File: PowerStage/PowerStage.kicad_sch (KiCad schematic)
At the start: 90 parts, among them J1 AH, J10 AH, J11 AH, J12 AH, J13 AH, J14 AH, J19 PhaseA, J2 AH, J20 PhaseB, J21 PhaseB, J22 AH, J23 AH, J24 AH, J25 AH, J3 BH, J4 BH, J5 BH, J6 CH, J7 CH, J8 CH, J9 AH, Q20 HY5110W, Q21 HY5110W, Q22 HY5110W, Q23 HY5110W, Q24 HY5110W, Q25 HY5110W, Q26 HY5110W, Q27 HY5110W, Q28 HY5110W, Q29 HY5110W, Q30 HY5110W, Q31 HY5110W, Q38 HY5110W, Q39 HY5110W, Q40 HY5110W, Q41 HY5110W, Q42 HY5110W, Q43 HY5110W

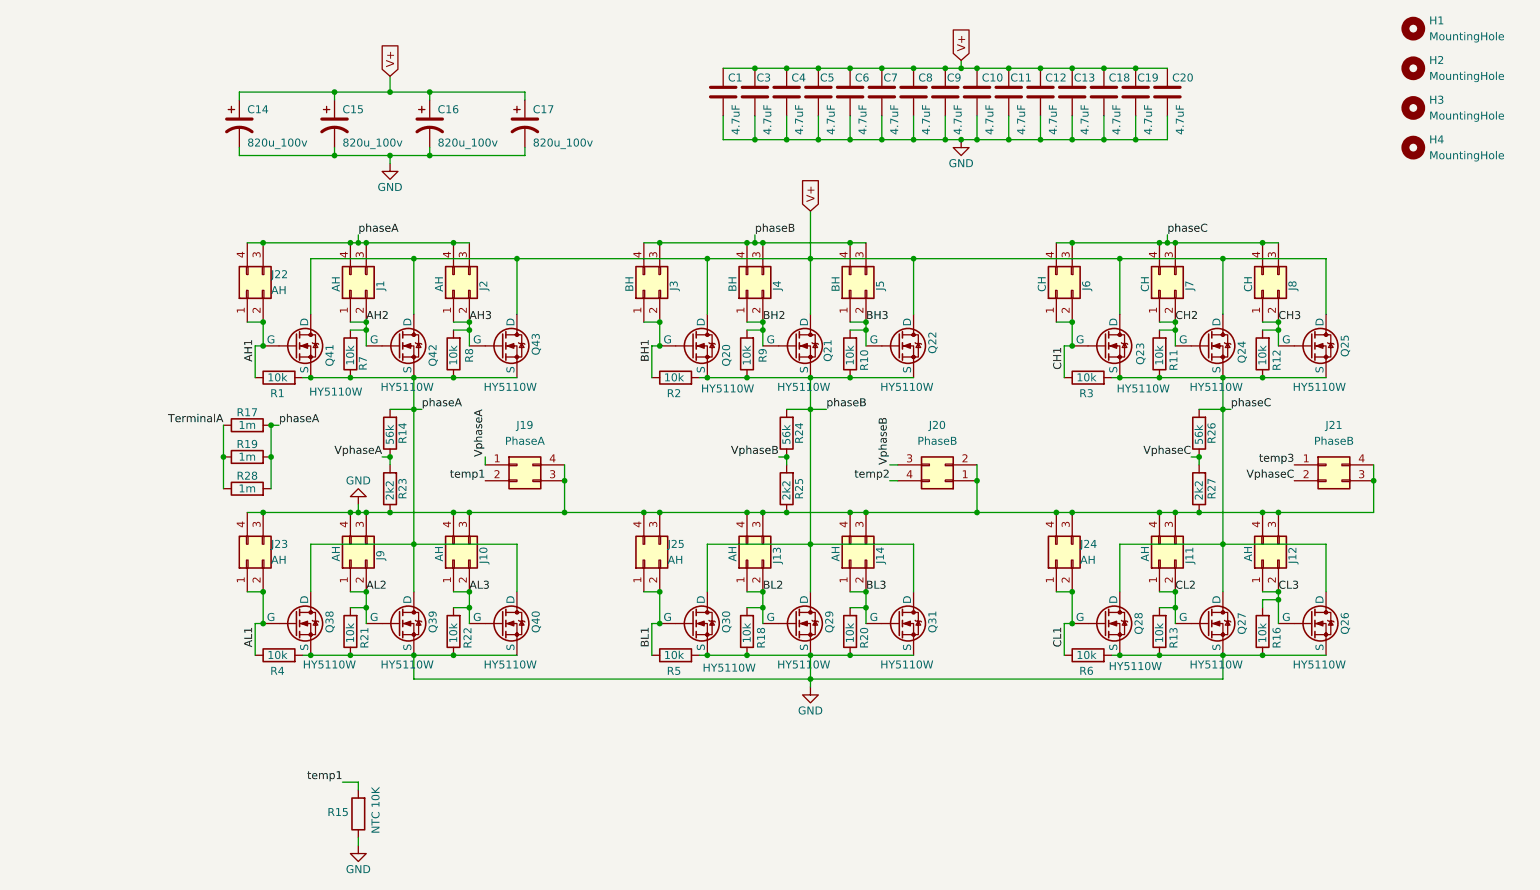
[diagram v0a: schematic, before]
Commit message: routing pinheader
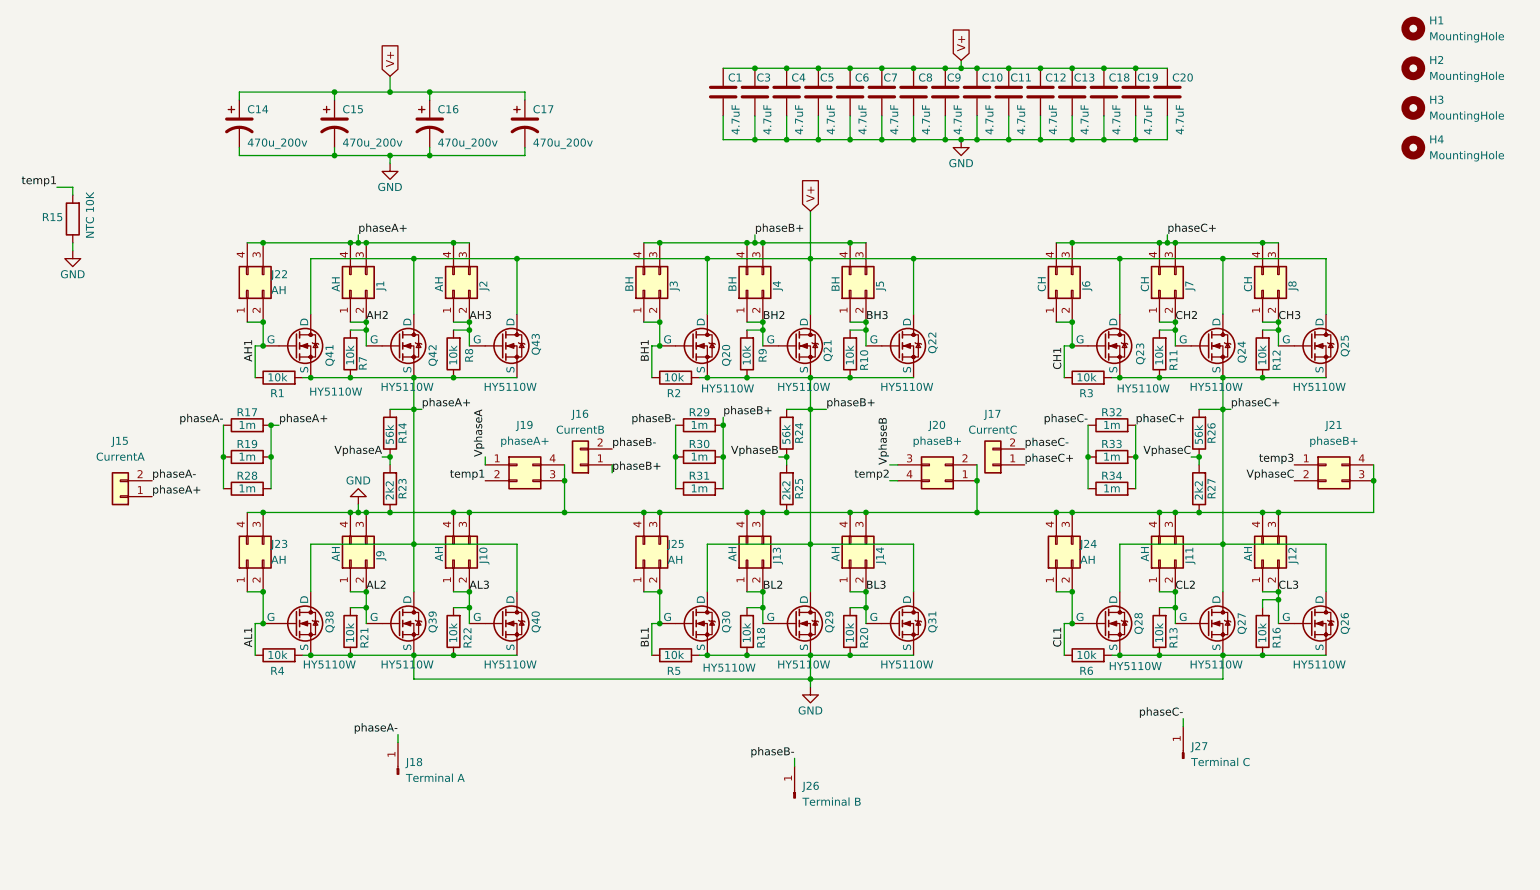
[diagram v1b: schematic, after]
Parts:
- added J15: CurrentA, Connector_PinSocket_2.54mm:PinSocket_1x02_P2.54mm_Vertical_SMD_Pin1Left, symbol Connector_Generic:Conn_01x02
- added J16: CurrentB, Connector_PinSocket_2.54mm:PinSocket_1x02_P2.54mm_Vertical_SMD_Pin1Left, symbol Connector_Generic:Conn_01x02
- added J17: CurrentC, Connector_PinSocket_2.54mm:PinSocket_1x02_P2.54mm_Vertical_SMD_Pin1Left, symbol Connector_Generic:Conn_01x02
- added J18: Terminal A, custom:225685-E, symbol Connector:Conn_01x01_Pin
- added J26: Terminal B, custom:225685-E, symbol Connector:Conn_01x01_Pin
- added J27: Terminal C, custom:225685-E, symbol Connector:Conn_01x01_Pin
- added R29, R30, R31, R32, R33, R34: 1m, custom:ShuntResistor_P2mmD10mm, symbol Device:R
- C14, C15, C16, C17: value 820u_100v -> 470u_200v; footprint Capacitor_THT:CP_Radial_D18.0mm_P7.50mm -> Capacitor_THT:CP_Radial_D25.0mm_P10.00mm_SnapIn
- J19: value PhaseA -> phaseA+
- J20, J21: value PhaseB -> phaseB+
- R17, R19, R28: footprint (none) -> custom:ShuntResistor_P2mmD10mm
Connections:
- net TerminalA renamed phaseA-
- net phaseA-: now also J15.2 (Pin_2), J18.1 (Pin_1)
- net phaseA renamed phaseA+
- net phaseA+: now also J15.1 (Pin_1)
- net phaseB renamed phaseB+
- net phaseB+: now also J16.1 (Pin_1), R29.2, R30.2, R31.2
- net phaseC renamed phaseC+
- net phaseC+: now also J17.1 (Pin_1), R32.2, R33.2, R34.2
- new net phaseB-: J16.2 (Pin_2), J26.1 (Pin_1), R29.1, R30.1, R31.1
- new net phaseC-: J17.2 (Pin_2), J27.1 (Pin_1), R32.1, R33.1, R34.1
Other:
- moved on the sheet: R15
